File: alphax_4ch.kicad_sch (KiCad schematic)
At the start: 247 parts, among them J1 USB_B_Mini, J2 Cortex_Debug, J3 Conn_01x01, J4 Conn_01x01, J5 Conn_01x01, J6 Conn_01x01, J7 Conn_01x01, J8 Conn_01x01, M1 Module-power12-0.2, M2 Module-power5-0.2, M3 Module-vr-discrete-0.1, M4 Module-ign8-0.2, M5 Module-input-0.1, M6 Module-mcu144-0.6, M7 Module-can-0.1, M8 Module-vr-discrete-0.1, M9 Module-knock-0.1, P1 33311-24AW-2, P2 33311-24AW-2, Q1 AO3400A, Q10 AO3400A, Q11 AO3400A, Q12 AO3400A, Q13 AO3401A, Q14 AO3401A, Q15 AO3400A, Q16 AO3401A, Q17 AO3401A, Q18 AO3401A, Q19 AO3400A, Q2 AO3400A, Q20 AO3400A, Q21 AO3400A, Q22 VND14NV04-E, Q23 VND14NV04-E, Q24 AO3400A, Q25 AO3400A, Q26 VND14NV04-E, Q27 AO3400A, Q28 VND14NV04-E, Q29 VND14NV04-E, Q3 AO3401A, Q30 VND14NV04-E, Q31 AO3401A, Q32 AO3401A, Q33 AO3400A, Q34 AO3400A, Q35 AO3400A, Q36 AO3400A, Q4 AO3401A, Q5 AO3401A, Q6 VND14NV04-E, Q7 VND14NV04-E, Q8 VND14NV04-E, Q9 VND14NV04-E, U1 TLS115, U2 74HC2G17GW, U3 MPXH6400A, U4 JDY-33, U5 74HC2G17GW, U6 TLE9201SG, U7 SN74LVC1G06DBVR

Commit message: rev.D draft
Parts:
- added C18: 22u, hellen-one-common:C0603, symbol hellen-one-common:Cap
- added J9: Micro_SD_Card, Connector_Card:microSD_HC_Wuerth_693072010801, symbol Connector:Micro_SD_Card
- added R96: 33k, hellen-one-common:R0603, symbol hellen-one-common:Res
- R47: value 2k -> 470; footprint hellen-one-common:R1206 -> hellen-one-common:R0805; LCSC C17944 -> C17710
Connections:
- net +3V3: now also C18.2, J9.4 (VDD), R96.1
- net GND: now also C18.1, J9.6 (VSS), J9.9 (SHIELD)
- net OUT_TACH: no longer D1.2 (A)
- net at D1.1 (K), R50.7, R50.8: no longer D9.1 (A)
- net SD_SCK: now reaches M6.N20 (SPI2_SCK)
- net SD_SCK: now also J9.2 (DAT3/CD)
- net SD_MISO: now reaches M6.N21 (SPI2_MISO)
- net SD_MISO: now also J9.7 (DAT0), R96.2
- net SD_MOSI: now reaches M6.N22 (SPI2_MOSI)
- net SD_MOSI: now also J9.3 (CMD)
- net SD_CS: now reaches M6.N23 (SPI2_CS)
- net SD_CS: now also J9.5 (CLK)
- new net: D1.2 (A), D9.1 (A)
- no-connect marks 76 -> 74
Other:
- note added: "BLACK"
- note added: "GREY"
- moved on the sheet: D1

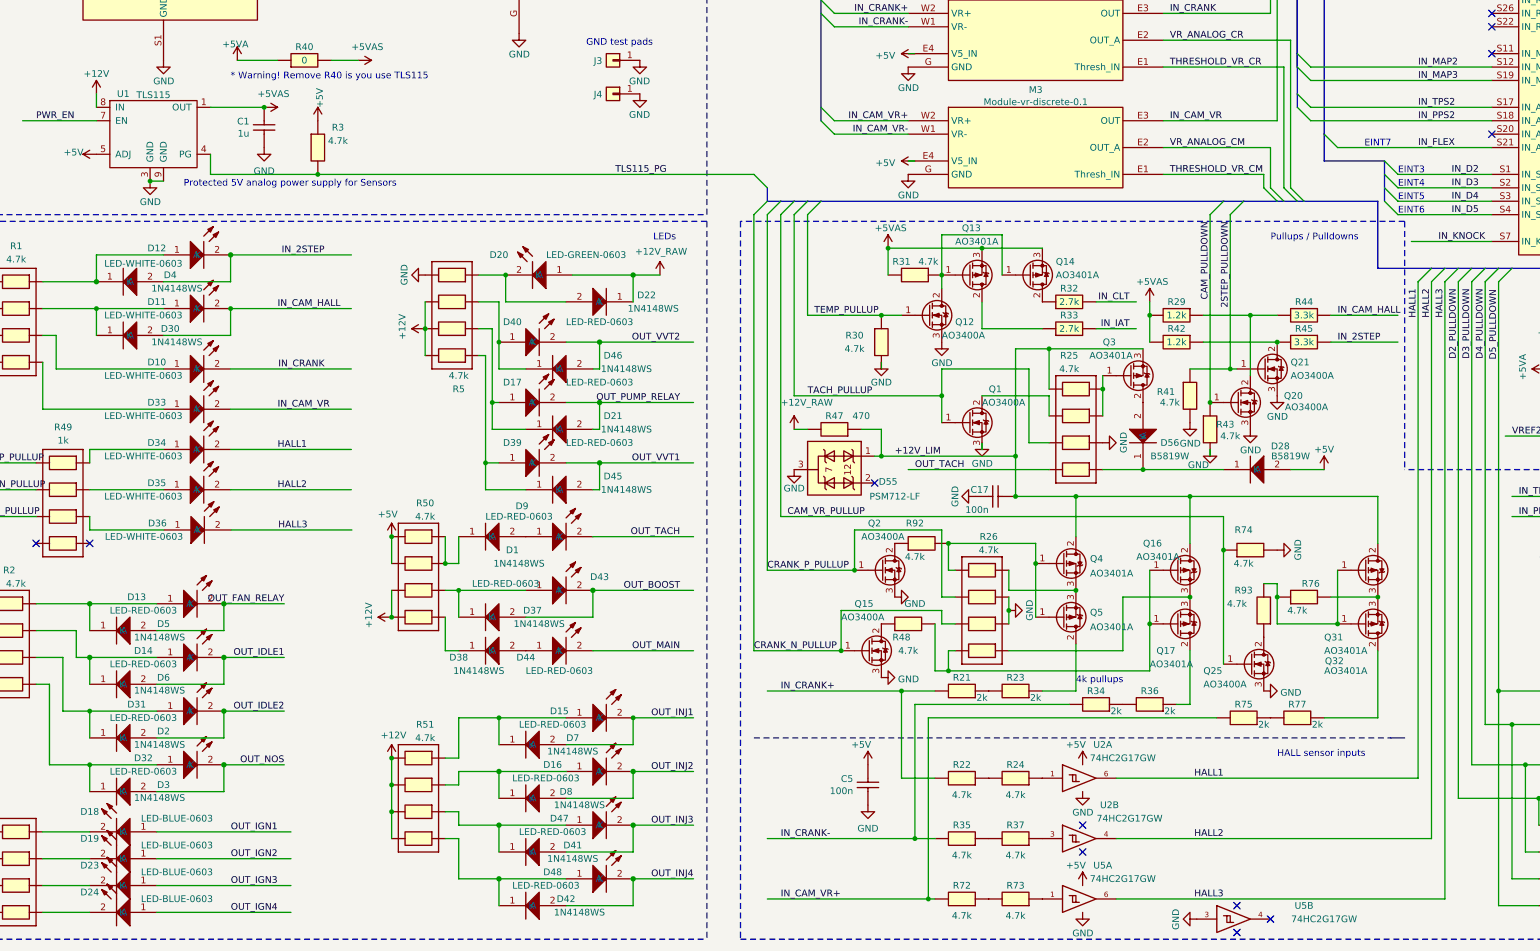
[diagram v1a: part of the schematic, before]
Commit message: rev.D: https://github.com/rusefi/alphax-4chan/issues/43 https://github.com/rusefi/alphax-4chan/issues/49
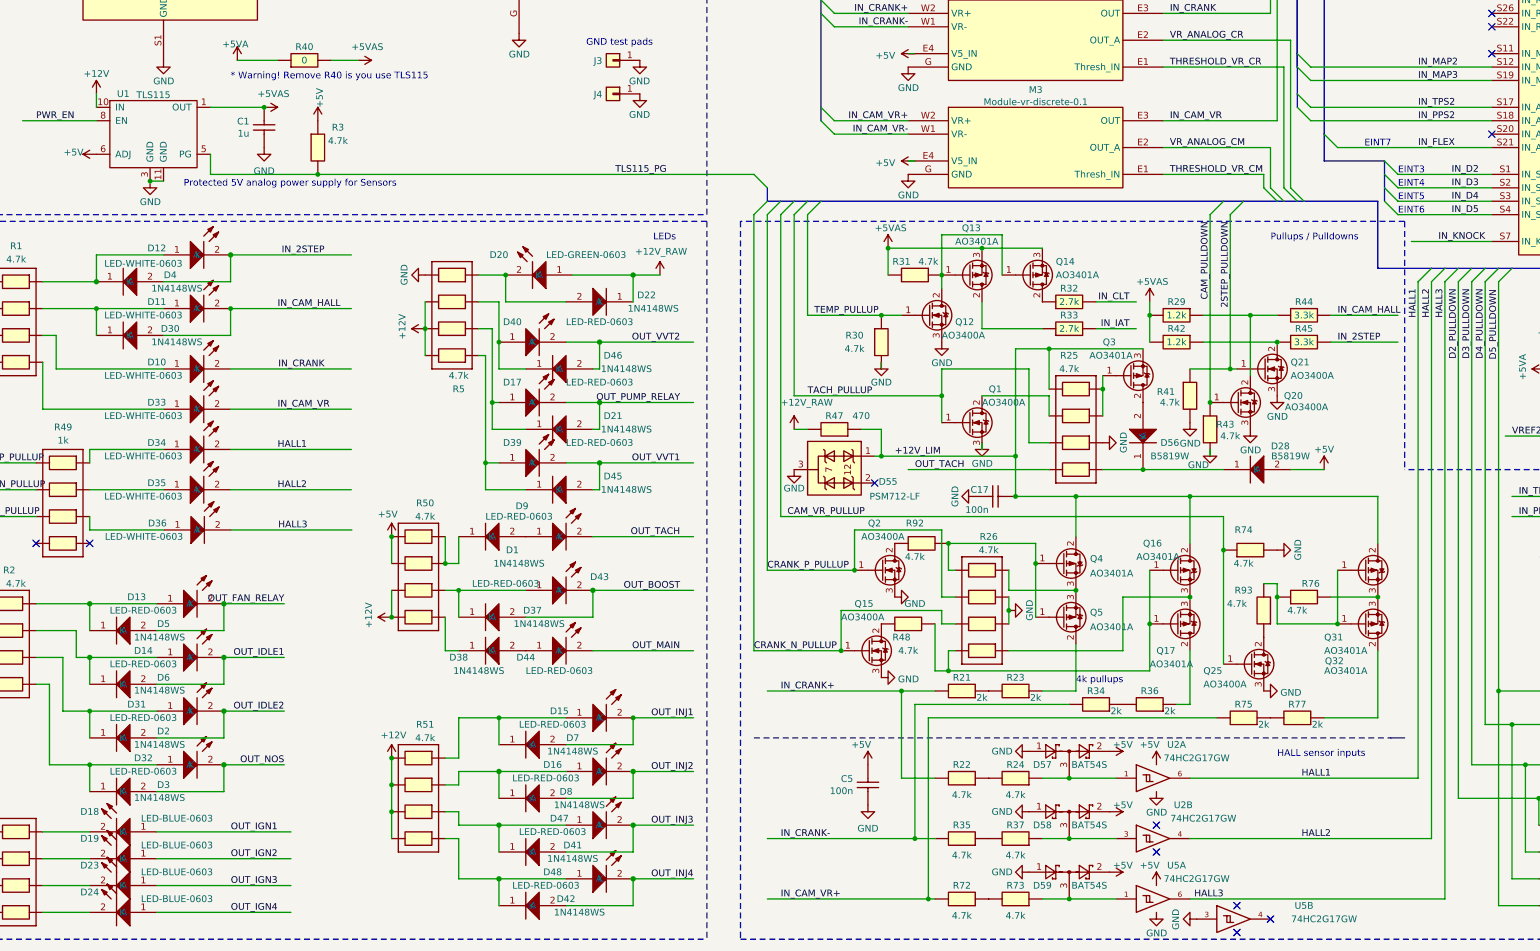
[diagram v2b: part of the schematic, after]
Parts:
- added D57, D58, D59: BAT54S, Package_TO_SOT_SMD:SOT-23, symbol Diode:BAT54S
- U1: footprint hellen-one-common:PG-DSO-8-43 -> hellen-one-common:PG-TSON-10-2; LCSC C540242 -> C9900011264; PN TLS115D0EJXUMA1 -> TLS115D0LDXUMA1
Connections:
- net +12V: now also U1.10 (IN); no longer U1.8 (IN)
- net +5V: now also U1.6 (ADJ), D57.2, D58.2, D59.2; no longer U1.5 (ADJ)
- net GND: now also U1.11 (GND), D57.1, D58.1, D59.1; no longer U1.9 (GND)
- net PWR_EN: now also U1.8 (EN); no longer U1.7 (EN)
- net TLS115_PG: now also U1.5 (PG); no longer U1.4 (PG)
- net at R37.1, U2.3: now also D58.3
- net at R73.1, U5.1: now also D59.3
- net at R24.1, U2.1: now also D57.3
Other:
- moved on the sheet: U2A, U2B, U5A

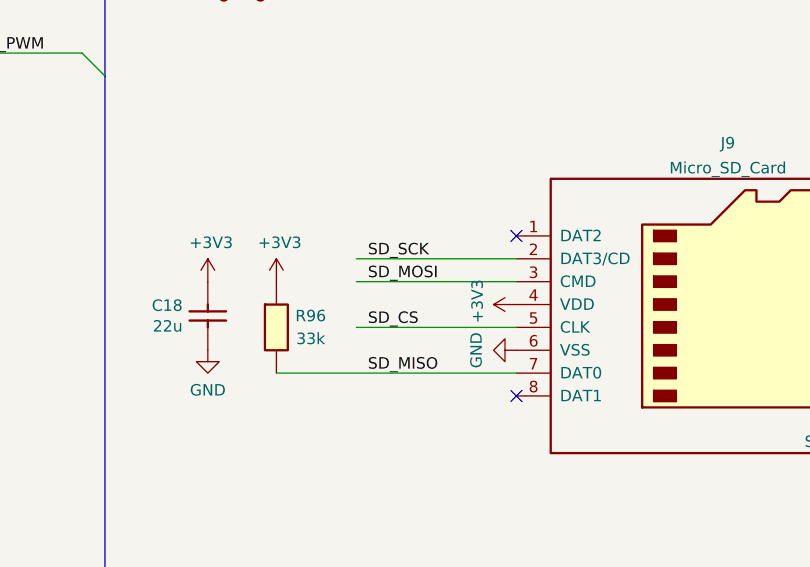
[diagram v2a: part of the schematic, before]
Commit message: rev.E draft + sd-card fix (#59)
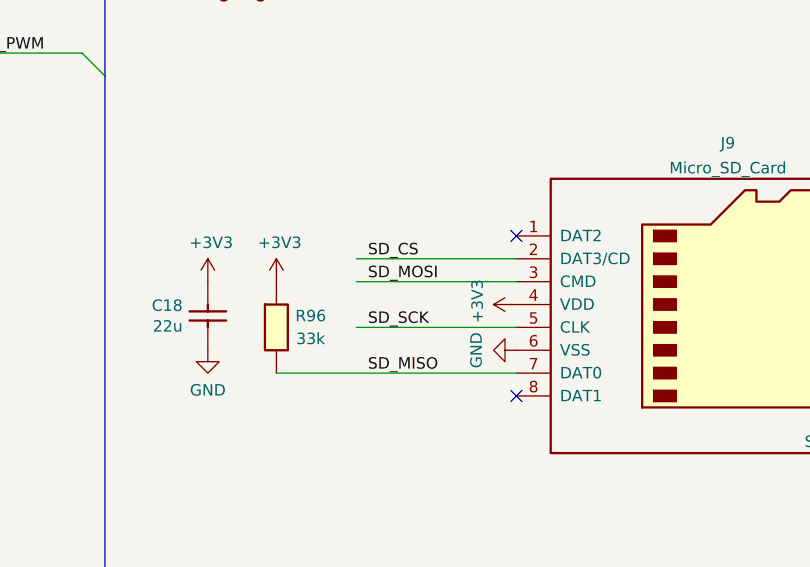
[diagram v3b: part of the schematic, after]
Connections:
- net SD_CS: now also J9.2 (DAT3/CD); no longer J9.5 (CLK)
- net SD_SCK: now also J9.5 (CLK); no longer J9.2 (DAT3/CD)
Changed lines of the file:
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@@
   (title_block
     (title "AlphaECU 4chan powered by rusEFI")
-    (date "2022-07-29")
-    (rev "D")
+    (date "2022-08-21")
+    (rev "E")
     (company "rusEFI")
     (comment 7 "http://rusefi.com/s/alphax4ch")
@@
     (effects (font (size 1.27 1.27)) (justify left bottom))
   )
-  (label "SD_CS" (at 506.73 219.71 0)
+  (label "SD_CS" (at 506.73 212.09 0)
     (effects (font (size 1.27 1.27)) (justify left bottom))
   )
@@
     (effects (font (size 1.27 1.27)) (justify right bottom))
   )
-  (label "SD_SCK" (at 506.73 212.09 0)
+  (label "SD_SCK" (at 506.73 219.71 0)
     (effects (font (size 1.27 1.27)) (justify left bottom))
   )

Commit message: #61
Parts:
- added J10, J11: Conn_01x01, TestPoint:TestPoint_Pad_D2.0mm, symbol Connector_Generic:Conn_01x01
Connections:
- net IN_CAM_HALL: now also J11.1 (Pin_1)
- net IN_CRANK: now also J10.1 (Pin_1)
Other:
- note added: "CRANK/CAM test pads"
- moved on the sheet: J3, J4
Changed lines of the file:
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@@
   (title_block
     (title "AlphaECU 4chan powered by rusEFI")
-    (date "2022-08-21")
+    (date "2022-09-05")
     (rev "E")
     (company "rusEFI")
@@
     (stroke (width 0) (type default) (color 0 0 0 0))
   )
+  (wire (pts (xy 149.86 232.41) (xy 161.29 232.41))
+    (stroke (width 0) (type default) (color 0 0 0 0))
+  )
   (wire (pts (xy 279.4 124.46) (xy 302.26 124.46))
     (stroke (width 0) (type default) (color 0 0 0 0))
@@
     (stroke (width 0) (type dash) (color 0 0 0 0))
   )
+  (wire (pts (xy 149.86 238.76) (xy 161.29 238.76))
+    (stroke (width 0) (type default) (color 0 0 0 0))
+  )
   (wire (pts (xy 121.92 105.41) (xy 96.52 105.41))
     (stroke (width 0) (type solid) (color 0 0 0 0))
@@
     (effects (font (size 1.27 1.27)) (justify left bottom))
   )
+  (text "CRANK/CAM test pads" (at 139.7 229.87 0)
+    (effects (font (size 1.27 1.27)) (justify left bottom))
+  )
   (text "ETB driver" (at 494.03 298.45 0)
     (effects (font (size 1.27 1.27)) (justify left bottom))
@@
     (effects (font (size 1.27 1.27)) (justify right bottom))
   )
-  (text "GND test pads" (at 139.7 236.22 0)
+  (text "GND test pads" (at 139.7 243.84 0)
     (effects (font (size 1.27 1.27)) (justify left bottom))
   )
@@
     (effects (font (size 1.27 1.27)) (justify right bottom))
   )
+  (label "IN_CAM_HALL" (at 149.86 238.76 0)
+    (effects (font (size 1.27 1.27)) (justify left bottom))
+  )
   (label "IDLE2" (at 394.97 92.71 0)
     (effects (font (size 1.27 1.27)) (justify left bottom))
@@
     (effects (font (size 1.27 1.27)) (justify left bottom))
   )
+  (label "IN_CRANK" (at 149.86 232.41 0)
+    (effects (font (size 1.27 1.27)) (justify left bottom))
+  )
   (label "OUT_ETB-" (at 187.96 154.94 180)
     (effects (font (size 1.27 1.27)) (justify right bottom))
@@
     (pin "2")
   )
-  (symbol (lib_id "power:GND") (at 149.86 245.11 0) (mirror y) (unit 1)
+  (symbol (lib_id "power:GND") (at 149.86 252.73 0) (mirror y) (unit 1)
     (in_bom yes) (on_board yes)
-    (property "Reference" "#PWR046" (id 0) (at 149.86 251.46 0)
+    (property "Reference" "#PWR046" (id 0) (at 149.86 259.08 0)
       (effects (font (size 1.27 1.27)) hide)
     )
-    (property "Value" "GND" (id 1) (at 149.8092 249.0534 0))
-    (property "Footprint" "" (id 2) (at 149.86 245.11 0)
+    (property "Value" "GND" (id 1) (at 149.8092 256.6734 0))
+    (property "Footprint" "" (id 2) (at 149.86 252.73 0)
       (effects (font (size 1.27 1.27)) hide)
     )
-    (property "Datasheet" "" (id 3) (at 149.86 245.11 0)
+    (property "Datasheet" "" (id 3) (at 149.86 252.73 0)
       (effects (font (size 1.27 1.27)) hide)
     )
@@
     (pin "2")
   )
-  (symbol (lib_id "power:GND") (at 149.86 238.76 0) (mirror y) (unit 1)
+  (symbol (lib_id "power:GND") (at 149.86 246.38 0) (mirror y) (unit 1)
     (in_bom yes) (on_board yes)
-    (property "Reference" "#PWR020" (id 0) (at 149.86 245.11 0)
+    (property "Reference" "#PWR020" (id 0) (at 149.86 252.73 0)
       (effects (font (size 1.27 1.27)) hide)
     )
-    (property "Value" "GND" (id 1) (at 149.8092 242.7034 0))
-    (property "Footprint" "" (id 2) (at 149.86 238.76 0)
+    (property "Value" "GND" (id 1) (at 149.8092 250.3234 0))
+    (property "Footprint" "" (id 2) (at 149.86 246.38 0)
       (effects (font (size 1.27 1.27)) hide)
     )
-    (property "Datasheet" "" (id 3) (at 149.86 238.76 0)
+    (property "Datasheet" "" (id 3) (at 149.86 246.38 0)
       (effects (font (size 1.27 1.27)) hide)
     )
@@
     (pin "1")
   )
-  (symbol (lib_id "Connector_Generic:Conn_01x01") (at 144.78 245.11 0) (mirror y) (unit 1)
+  (symbol (lib_id "Connector_Generic:Conn_01x01") (at 144.78 252.73 0) (mirror y) (unit 1)
     (in_bom yes) (on_board yes)
-    (property "Reference" "J4" (id 0) (at 142.748 245.2116 0)
+    (property "Reference" "J4" (id 0) (at 142.748 252.8316 0)
       (effects (font (size 1.27 1.27)) (justify left))
     )
-    (property "Value" "Conn_01x01" (id 1) (at 142.748 246.3546 0)
+    (property "Value" "Conn_01x01" (id 1) (at 142.748 253.9746 0)
       (effects (font (size 1.27 1.27)) (justify left) hide)
     )
-    (property "Footprint" "TestPoint:TestPoint_Pad_D2.0mm" (id 2) (at 144.78 245.11 0)
+    (property "Footprint" "TestPoint:TestPoint_Pad_D2.0mm" (id 2) (at 144.78 252.73 0)
       (effects (font (size 1.27 1.27)) hide)
     )
-    (property "Datasheet" "~" (id 3) (at 144.78 245.11 0)
+    (property "Datasheet" "~" (id 3) (at 144.78 252.73 0)
       (effects (font (size 1.27 1.27)) hide)
     )
@@
     (pin "2")
   )
+  (symbol (lib_id "Connector_Generic:Conn_01x01") (at 144.78 232.41 0) (mirror y) (unit 1)
+    (in_bom yes) (on_board yes)
+    (property "Reference" "J10" (id 0) (at 142.748 232.5116 0)
+      (effects (font (size 1.27 1.27)) (justify left))
+    )
+    (property "Value" "Conn_01x01" (id 1) (at 142.748 233.6546 0)
+      (effects (font (size 1.27 1.27)) (justify left) hide)
+    )
+    (property "Footprint" "TestPoint:TestPoint_Pad_D2.0mm" (id 2) (at 144.78 232.41 0)
+      (effects (font (size 1.27 1.27)) hide)
+    )
+    (property "Datasheet" "~" (id 3) (at 144.78 232.41 0)
+      (effects (font (size 1.27 1.27)) hide)
+    )
+    (pin "1")
+  )
   (symbol (lib_id "hellen-one-common:MOSFET-N") (at 278.13 173.99 0) (mirror y) (unit 1)
     (in_bom yes) (on_board yes)
@@
     (pin "9")
   )
-  (symbol (lib_id "Connector_Generic:Conn_01x01") (at 144.78 238.76 0) (mirror y) (unit 1)
+  (symbol (lib_id "Connector_Generic:Conn_01x01") (at 144.78 246.38 0) (mirror y) (unit 1)
     (in_bom yes) (on_board yes)
-    (property "Reference" "J3" (id 0) (at 142.748 238.8616 0)
+    (property "Reference" "J3" (id 0) (at 142.748 246.4816 0)
       (effects (font (size 1.27 1.27)) (justify left))
     )
-    (property "Value" "Conn_01x01" (id 1) (at 142.748 240.0046 0)
+    (property "Value" "Conn_01x01" (id 1) (at 142.748 247.6246 0)
       (effects (font (size 1.27 1.27)) (justify left) hide)
     )
-    (property "Footprint" "TestPoint:TestPoint_Pad_D2.0mm" (id 2) (at 144.78 238.76 0)
+    (property "Footprint" "TestPoint:TestPoint_Pad_D2.0mm" (id 2) (at 144.78 246.38 0)
       (effects (font (size 1.27 1.27)) hide)
     )
-    (property "Datasheet" "~" (id 3) (at 144.78 238.76 0)
+    (property "Datasheet" "~" (id 3) (at 144.78 246.38 0)
       (effects (font (size 1.27 1.27)) hide)
     )
@@
     (pin "3")
   )
+  (symbol (lib_id "Connector_Generic:Conn_01x01") (at 144.78 238.76 0) (mirror y) (unit 1)
+    (in_bom yes) (on_board yes)
+    (property "Reference" "J11" (id 0) (at 142.748 238.8616 0)
+      (effects (font (size 1.27 1.27)) (justify left))
+    )
+    (property "Value" "Conn_01x01" (id 1) (at 142.748 240.0046 0)
+      (effects (font (size 1.27 1.27)) (justify left) hide)
+    )
+    (property "Footprint" "TestPoint:TestPoint_Pad_D2.0mm" (id 2) (at 144.78 238.76 0)
+      (effects (font (size 1.27 1.27)) hide)
+    )
+    (property "Datasheet" "~" (id 3) (at 144.78 238.76 0)
+      (effects (font (size 1.27 1.27)) hide)
+    )
+    (pin "1")
+  )
   (symbol (lib_id "hellen-one-power12-0.2:Module-power12-0.2") (at 44.45 210.82 0) (unit 1)
     (in_bom yes) (on_board yes) (fields_autoplaced)
@@
       (reference "J9") (unit 1) (value "Micro_SD_Card") (footprint "Connector_Card:microSD_HC_Wuerth_693072010801")
     )
+    (path "/6a1b9761-b99d-45be-a065-b90f76ff7b92"
+      (reference "J10") (unit 1) (value "Conn_01x01") (footprint "TestPoint:TestPoint_Pad_D2.0mm")
+    )
+    (path "/ec6fd702-be7d-4727-b414-2cd56ebf615a"
+      (reference "J11") (unit 1) (value "Conn_01x01") (footprint "TestPoint:TestPoint_Pad_D2.0mm")
+    )
     (path "/ece5d7d1-76db-401f-8553-a51e2efb44d2"

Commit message: rev.F
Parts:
- removed M3, M8: Module-vr-discrete-0.1, hellen-one-vr-discrete-0.1:vr-discrete, symbol vr-discrete:Module-vr-discrete-0.1
- removed R13, R14, R20, R57, R58, R6, R65, R66, R7, R71: Jumper-Pad-Pad, hellen-one-common:PAD-0805-PAD, symbol hellen-one-common:Jumper-Pad-Pad
- added M3, M8: Module-vr-discrete-0.4, hellen-one-vr-discrete-0.4:vr-discrete, symbol vr-discrete-0.4:Module-vr-discrete-0.4
- M9: value Module-knock-0.1 -> Module-knock-0.2; footprint hellen-one-knock-0.1:knock -> hellen-one-knock-0.2:knock; symbol hellen-one-knock-0.1:Module-knock-0.1 -> hellen-one-knock-0.2:Module-knock-0.2
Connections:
- net A8 is gone; now on net OUT_INJ1: P1.8 (A8)
- net B8 is gone; now on net OUT_INJ2: P1.16 (B8)
- net C1 is gone; now on net OUT_FAN_RELAY: P1.17 (C1)
- net C7 is gone; now on net IN_CAM_HALL: P1.23 (C7)
- net C8 is gone; now on net OUT_IDLE1: P1.24 (C8)
- net E1 is gone; now on net OUT_INJ4: P2.9 (E1)
- net E2 is gone; now on net OUT_NOS: P2.10 (E2)
- net F1 is gone; now on net OUT_IDLE2: P2.17 (F1)
- net F2 is gone; now on net OUT_VVT1: P2.18 (F2)
- net OUT_INJ3 is gone; now on net D1: D41.2 (A), D47.2 (K), Q26.2 (D)
- net +5V: now also M3.E4 (V5_IN), M8.E4 (V5_IN)
- net GND: now also M3.G (GND), M8.G (GND)
- net IN_CAM_VR: now also M3.E3 (OUT)
- net IN_CAM_VR+: now also M3.W2 (VR+)
- net IN_CAM_VR-: now also M3.W1 (VR-)
- net IN_CRANK: now also M8.E3 (OUT)
- net IN_CRANK+: now also M8.W2 (VR+)
- net IN_CRANK-: now also M8.W1 (VR-)
- net THRESHOLD_VR_CM: now also M3.E1 (Thresh_IN)
- net THRESHOLD_VR_CR: now also M8.E1 (Thresh_IN)
- net VR_ANALOG_CM: now also M3.E2 (OUT_A)
- net VR_ANALOG_CR: now also M8.E2 (OUT_A)
- net at U3.1: now also U3.5, U3.6, U3.7, U3.8
- no-connect marks 74 -> 69
